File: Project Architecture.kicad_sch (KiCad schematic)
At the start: 0 parts

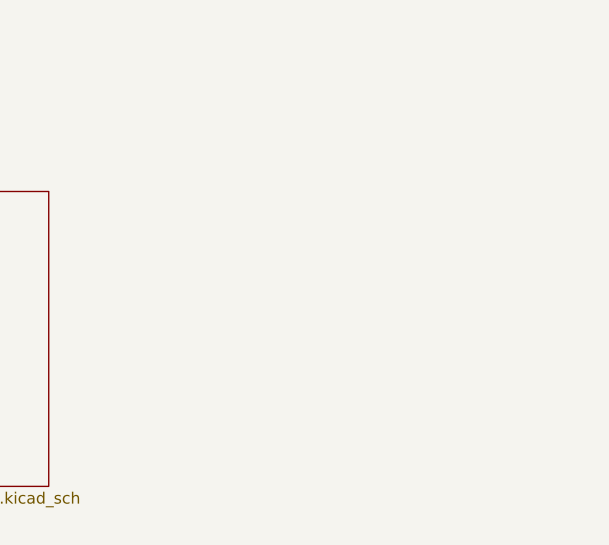
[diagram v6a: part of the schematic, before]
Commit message: Add FRAM
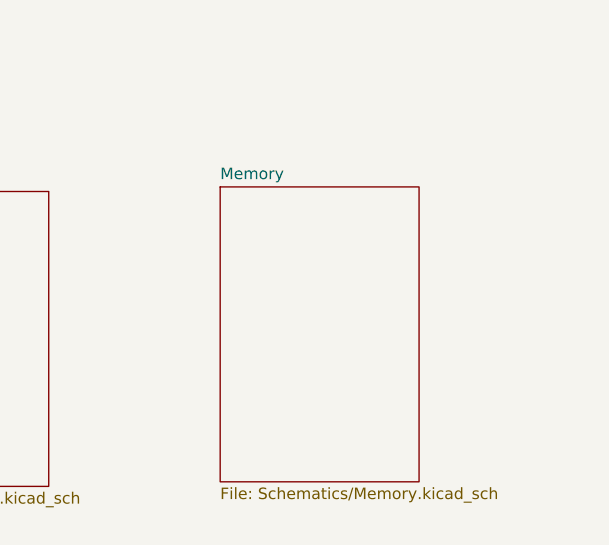
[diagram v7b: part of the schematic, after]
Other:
- added sheet Memory (Schematics/Memory.kicad_sch)
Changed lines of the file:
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@@
+	)
+	(sheet
+		(at 325.374 145.288)
+		(size 22.098 32.766)
+		(exclude_from_sim no)
+		(in_bom yes)
+		(on_board yes)
+		(dnp no)
+		(fields_autoplaced yes)
+		(stroke
+			(width 0.1524)
+			(type solid)
+		)
+		(fill
+			(color 0 0 0 0)
+		)
+		(property "Sheetname" "Memory"
+			(at 325.374 144.5764 0)
+			(show_name no)
+			(do_not_autoplace no)
+			(effects
+				(font
+					(size 1.27 1.27)
+				)
+				(justify left bottom)
+			)
+		)
+		(property "Sheetfile" "Schematics/Memory.kicad_sch"
+			(at 325.374 178.6386 0)
+			(show_name no)
+			(do_not_autoplace no)
+			(effects
+				(font
+					(size 1.27 1.27)
+				)
+				(justify left top)
+			)
+		)
+		(instances
+			(project "SkyForge_Controller"
+				(path "/0650c7a8-acba-429c-9f8e-eec0baf0bc1c/fede4c36-00cc-4d3d-b71c-5243ba232202"
+					(page "14")
+				)
+			)
+		)
 	)
 	(sheet
